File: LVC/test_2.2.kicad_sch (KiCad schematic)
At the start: 5 parts, among them U1 TL431DBZ

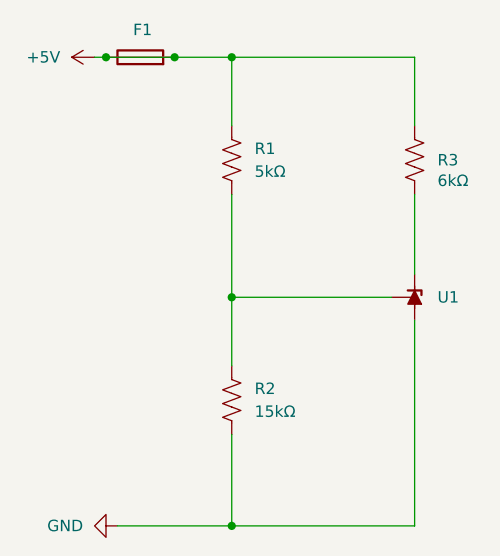
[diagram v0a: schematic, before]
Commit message: Refining Schematics
Refined the visuals of all the schematics to remove values from components. Also removed a redundant schematic.
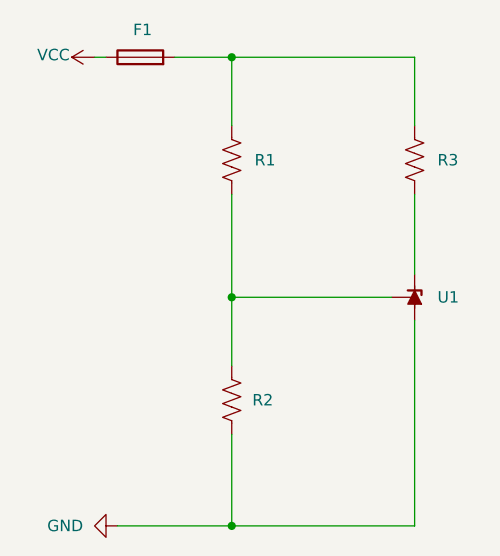
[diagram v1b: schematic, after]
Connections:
- net +5V: no longer F1.2, R1.1, R3.1
- new net: F1.2, R1.1, R3.1
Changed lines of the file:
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@@
-	)
-	(junction
-		(at 76.2 52.07)
-		(diameter 0)
-		(color 0 0 0 0)
 	)
 	(junction
@@
 	)
 	(junction
-		(at 83.82 52.07)
-		(diameter 0)
-		(color 0 0 0 0)
-	)
-	(junction
 		(at 90.17 104.14)
 		(diameter 0)
@@
 		(pts
 			(xy 107.95 78.74) (xy 90.17 78.74)
-		)
-		(stroke
-			(width 0)
-			(type default)
-		)
-	)
-	(wire
-		(pts
-			(xy 76.2 52.07) (xy 83.82 52.07)
 		)
 		(stroke
@@
 		(in_pos_files yes)
 		(dnp no)
-		(fields_autoplaced yes)
 		(property "Reference" "R2"
-			(at 92.71 88.8999 0)
+			(at 92.456 90.17 0)
 			(show_name no)
 			(do_not_autoplace no)
@@
 		(property "Value" "15kΩ"
 			(at 92.71 91.4399 0)
+			(hide yes)
 			(show_name no)
 			(do_not_autoplace no)
@@
 		(property "Value" "6kΩ"
 			(at 113.03 65.786 0)
+			(hide yes)
 			(show_name no)
 			(do_not_autoplace no)
@@
 		(fields_autoplaced yes)
 		(property "Reference" "R1"
-			(at 92.71 62.2299 0)
+			(at 92.71 63.4999 0)
 			(show_name no)
 			(do_not_autoplace no)
@@
 		(property "Value" "5kΩ"
 			(at 92.71 64.7699 0)
+			(hide yes)
 			(show_name no)
 			(do_not_autoplace no)
@@
 		(in_pos_files yes)
 		(dnp no)
-		(fields_autoplaced yes)
-		(property "Reference" "#PWR05"
-			(at 78.74 52.07 0)
-			(hide yes)
+		(property "Reference" "VCC"
+			(at 70.358 51.816 90)
 			(show_name no)
 			(do_not_autoplace no)
@@
 		(property "Value" "+5V"
 			(at 71.12 52.0699 90)
+			(hide yes)
 			(show_name no)
 			(do_not_autoplace no)
@@
 			(project "LVC"
 				(path "/e8c89e13-2fc2-40fb-b5c1-4374b244dd0a"
-					(reference "#PWR05")
+					(reference "VCC")
 					(unit 1)
 				)
